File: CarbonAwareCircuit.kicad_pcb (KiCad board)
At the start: 2 copper layers, 64 x 55.5 mm, 14 parts, among them J1 USB_C_Receptacle_USB2.0_14P, J2 USB_A, Q1 AO3401A, SW1 SW_Push, SW2 SW_Push, U1 LD1117V, U2 ESP32-C3-WROOM-02

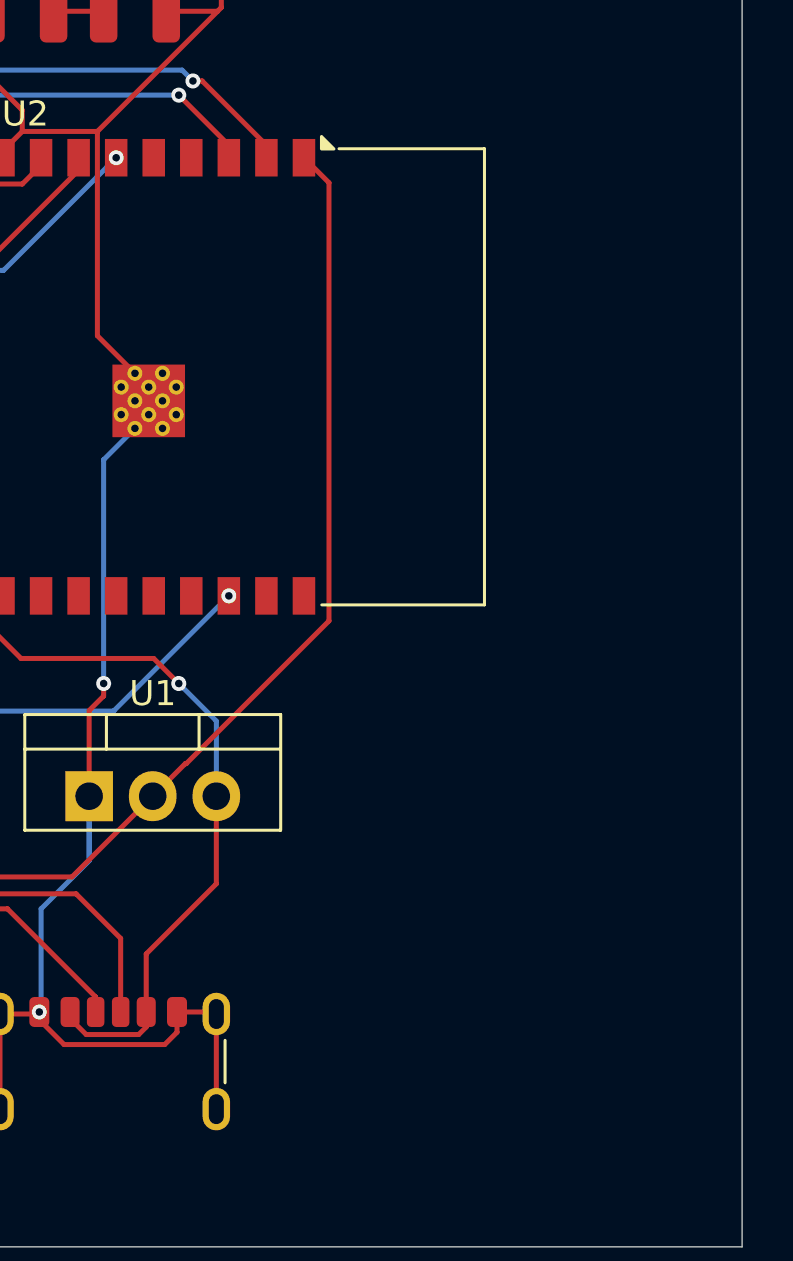
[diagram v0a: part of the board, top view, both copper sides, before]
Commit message: added silkscreen
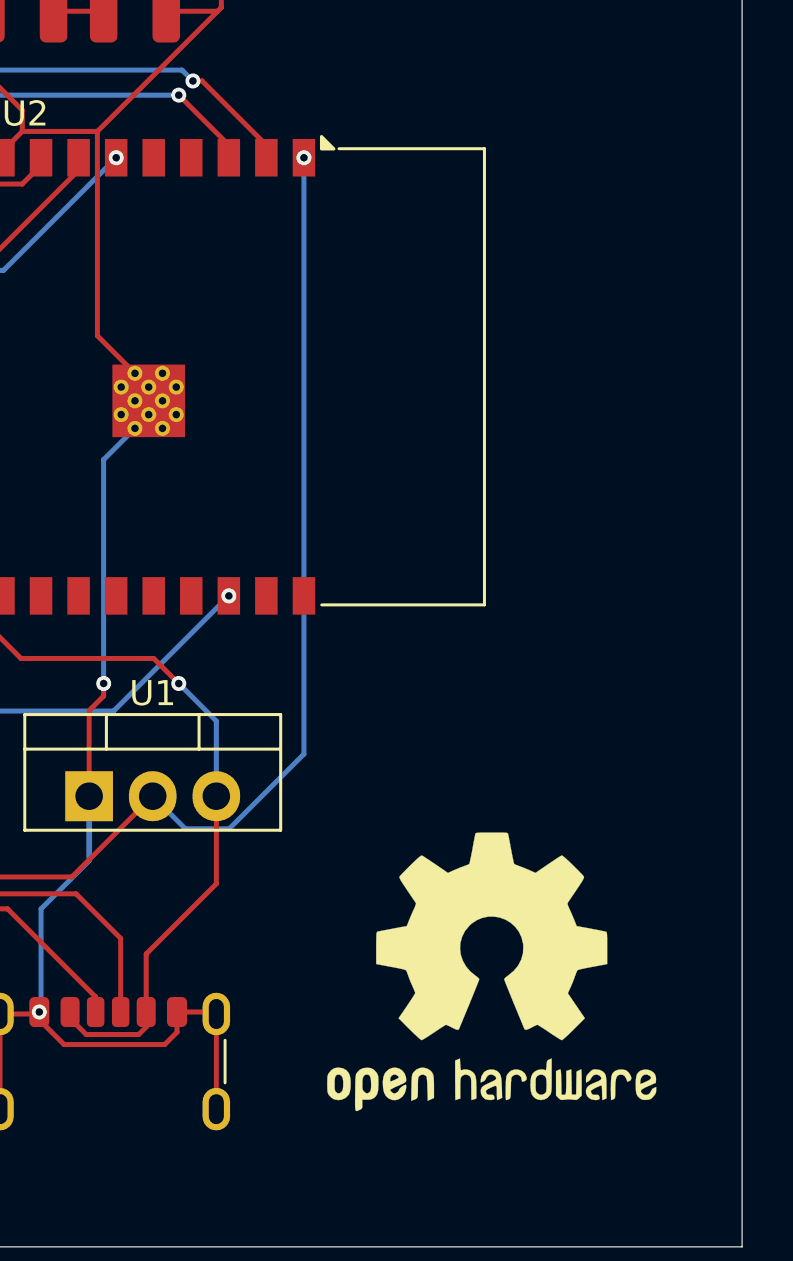
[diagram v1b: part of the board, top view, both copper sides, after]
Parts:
- added REF**: OSHW-Logo2_14.6x12mm_SilkScreen, Symbol:OSHW-Logo2_14.6x12mm_SilkScreen, F.Cu at (246.0, 132.5)
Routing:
- net Net-(U1-VO): track 55.6 -> 58.4 mm, vias 0 -> 1
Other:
- board text added: "Designed by Abhiram Vadali - CompSci Team C6"
